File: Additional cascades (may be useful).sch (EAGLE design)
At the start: 91 parts, among them J1 S7B-PH-K

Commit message: some edits
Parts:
- removed C1, C2: 33u/50V, resistor:C-EUC0603
- removed C10, C11, C4, C6, C7, C9: 2.2u/16V, resistor:C-EUC0603
- removed C12, C14, C15, C16, C17, C18, C19, C29, C30, C44, C45: 1u/16V, resistor:C-EUC0603
- removed C13, C34, C39, C49: 2200p, resistor:C-EUC0603
- removed C20, C21, C22, C23, C24, C25: 0.1u/100V, resistor:C-EUC0603
- removed C26, C27, C31, C33, C40, C41, C43, C47, C48, C55: 0.47u/16V, resistor:C-EUC0603
- removed C28, C32, C42, C46: 0.33u/16V, resistor:C-EUC0603
- removed C3: 2.2u/10V, resistor:C-EUC0603
- removed C37, C38, C5, C8: 51p, resistor:C-EUC0603
- removed D4, D5, D6, D7, D8, D9: BAT60J, diode:BAT60J
- removed J1: S7B-PH-K, con-jst-ph:B7B-PH-K
- removed R1, R23, R24, R25, R26, R27, R28, R29: 47, resistor:R-EU_R0603
- removed R10, R11, R4, R5: 49, resistor:R-EU_R0603
- removed R17, R18, R19, R20, R21, R22: 1k, resistor:R-EU_R0603
- removed R2: 100, resistor:R-EU_R0603
- removed R3, R9: 10k, resistor:R-EU_R0603
- removed R30, R31, R32, R33, R34, R35, R36: 10, 1/4W, resistor:R-EU_R0603
- removed R6: 100k, resistor:R-EU_R0603
- removed TP1, TP2: TEST_PAD, testing:TEST_PAD
- removed U$1: BQ79606A-Q1-HTQFP(PHP)|48, texas Instrumets:BQ79606A-Q1-HTQFP(PHP)|48
- removed U$2, U$3: S4B-PH-K, con-jst-ph:S4B-PH-K
- removed U$4, U$5: PESD2CAN, stmicroelectronics:PESD2CAN
- added C35, C36: 1u/16V, resistor:C-EUC0603
- added D1: (no value), eagle-ltspice:DIODE_E-
- added Q1: BSS123, transistor-small-signal:BSS123
- added R100, R8: 100, resistor:R-EU_R0603
- added R7: 1k, resistor:R-EU_R0603
- added RB: 20, resistor:R-EU_R0603
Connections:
- removed net COMLN: C38.1, R11.1, R9.1, U$1.COMLN
- removed net COMLP: C37.2, R10.1, R9.2, U$1.COMLP
- removed net GND: C1.1, C10.2, C11.2, C12.2, C14.1, C15.1, C16.1, C17.1, C18.1, C19.1, C2.2, C3.2, C37.1, C38.2, C4.2, C40.1, C5.1, C55.1, C6.2, C7.2, C8.2, C9.2, D4.A, D5.A, D6.A, D7.A, D8.A, D9.A, J1.1, R6.1, U$1.AVSS@0, U$1.AVSS@1, U$1.CVSS, U$1.DVSS
- removed net N$1: R2.1, U$1.BAT
- removed net N$10: C22.1, C23.2, J1.4, R26.1, R33.1
- removed net N$11: C23.1, C24.2, J1.3, R27.1, R34.1
- removed net N$12: C24.1, C25.2, J1.2, R28.1, R35.1, TP1.P$1
- removed net N$13: C26.1, C27.2, C28.2, R24.2, U$1.VC5
- removed net N$14: C27.1, C28.1, C29.2, R25.2, U$1.VC4
- removed net N$15: C29.1, C30.2, R26.2, U$1.VC3
- removed net N$16: C30.1, C31.2, C32.2, R27.2, U$1.VC2
- removed net N$17: C31.1, C32.1, C33.2, R28.2, TP2.P$1, U$1.VC1
- removed net N$18: C33.1, C40.2, R29.2, U$1.VC0
- removed net N$19: C42.1, C43.1, C44.2, R32.2, U$1.CB4
- removed net N$2: R1.1, U$1.LDOIN
- removed net N$20: C44.1, C45.2, R33.2, U$1.CB3
- removed net N$21: C45.1, C46.2, C47.2, R34.2, U$1.CB2
- removed net N$22: C3.1, U$1.TSREF
- removed net N$23: C48.1, C55.2, R36.2, U$1.CB0
- removed net N$24: C41.1, C42.2, C43.2, R31.2, U$1.CB5
- removed net N$25: C25.1, R29.1, R36.1
- removed net N$26: C26.2, R23.2, U$1.VC6
- removed net N$27: C20.1, C21.2, J1.6, R24.1, R31.1
- removed net N$28: C46.1, C47.1, C48.2, R35.2, U$1.CB1
- removed net N$29: C14.2, D9.C, R17.1, U$1.GIPO1
- removed net N$3: C11.1, C7.1, C9.1, U$1.CVDD, U$1.VIO, U$1.VLDO
- removed net N$30: C19.2, D4.C, R22.1, U$1.GIPO6
- removed net N$31: C18.2, D5.C, R21.1, U$1.GIPO5
- removed net N$32: C17.2, D6.C, R20.1, U$1.GIPO4
- removed net N$33: C16.2, D7.C, R19.1, U$1.GIPO3
- removed net N$34: C15.2, D8.C, R18.1, U$1.GIPO2
- removed net N$35: C5.2, R3.2, R4.1, U$1.FAULTLP
- removed net N$36: C8.1, R3.1, R5.1, U$1.FAULTLN
- removed net N$37: C13.2, R5.2
- removed net N$38: C34.2, R4.2
- removed net N$39: C34.1, U$2.1
- removed net N$4: C6.1, U$1.AVDD
- removed net N$40: C13.1, U$2.2
- removed net N$49: C39.2, R11.2
- removed net N$5: C10.1, U$1.DVDD
- removed net N$50: C49.2, R10.2
- removed net N$51: C49.1, U$2.3
- removed net N$52: C39.1, U$2.4
- removed net N$6: C4.1, U$1.REF1
- removed net N$7: C12.1, R6.2, U$1.VPROG
- removed net N$8: C41.2, R30.2, U$1.CB6
- removed net N$9: C21.1, C22.2, J1.5, R25.1, R32.1
- removed net VCC: C1.2, C2.1, C20.2, J1.7, R1.2, R2.2, R23.1, R30.1
- new net N$41: Q1.D, RB.1
- new net N$42: R100.1, RB.2
- new net N$43: C35.2, R100.2
- new net N$44: C35.1, R7.2, R8.2
- new net N$45: C36.1, D1.C, Q1.S, R8.1
- new net N$46: C36.2, D1.A, Q1.G, R7.1
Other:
- note added: "Maximum balance current is 150mA. Connect external MOSFET to have bigger balance-current"
- note added: "external MOSFET cell balancing example"
- note removed: "Connect GIPO through 10k resistor to AVSS if unused"
- note removed: "different PCB with less than 2m wiring"
- note removed: "left COM** and FAULT** (8pins total) unconected if not used"
- note removed: "same PCB config."

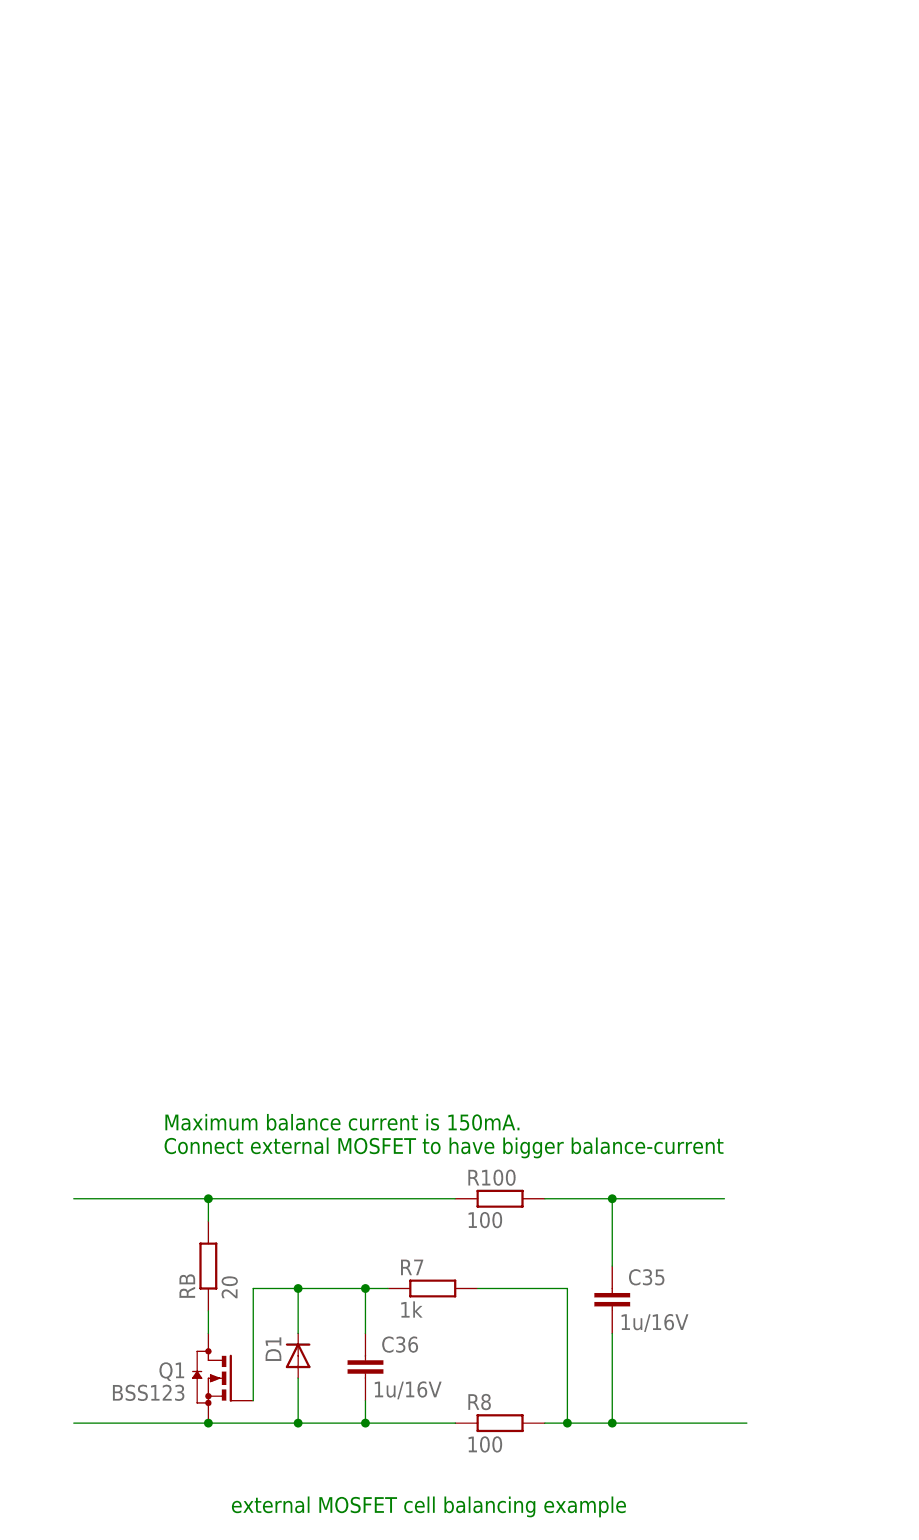
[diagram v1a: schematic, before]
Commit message: Board size to chek
The schematic file is close to release ver.
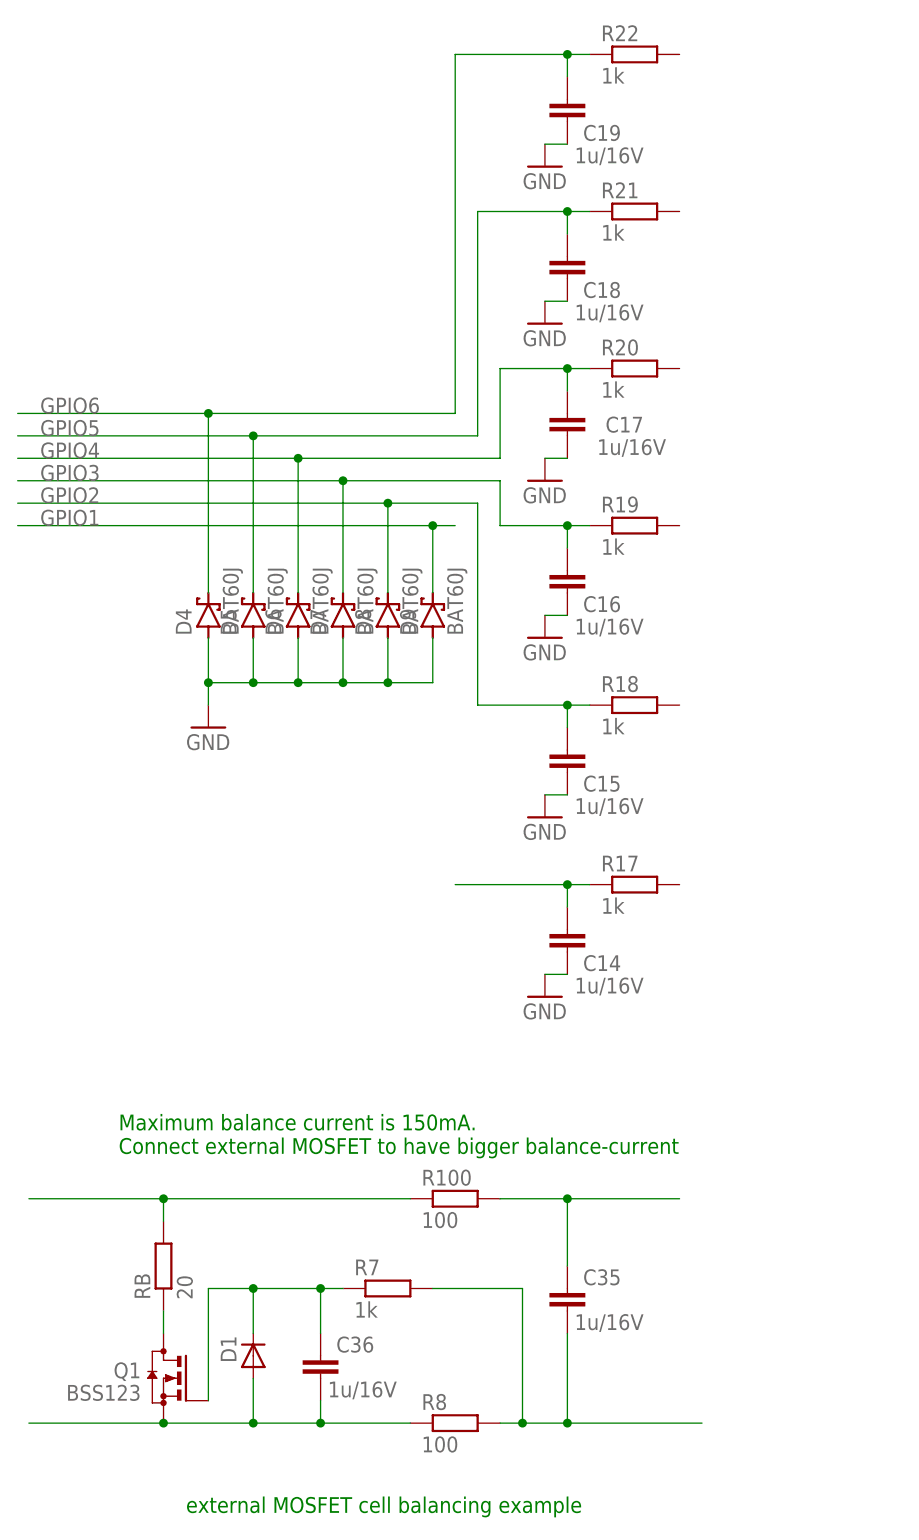
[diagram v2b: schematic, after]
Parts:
- added C14, C15, C16, C17, C18, C19: 1u/16V, resistor:C-EUC0603
- added D4, D5, D6, D7, D8, D9: BAT60J, diode:BAT60J
- added R17, R18, R19, R20, R21, R22: 1k, resistor:R-EU_R0603
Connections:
- new net GND: C14.1, C15.1, C16.1, C17.1, C18.1, C19.1, D4.A, D5.A, D6.A, D7.A, D8.A, D9.A
- new net GPIO1: C14.2, D9.C, R17.1
- new net GPIO2: C15.2, D8.C, R18.1
- new net GPIO3: C16.2, D7.C, R19.1
- new net GPIO4: C17.2, D6.C, R20.1
- new net GPIO5: C18.2, D5.C, R21.1
- new net GPIO6: C19.2, D4.C, R22.1
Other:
- moved on the sheet: C35, C36, D1, Q1, R100, R7, R8, RB

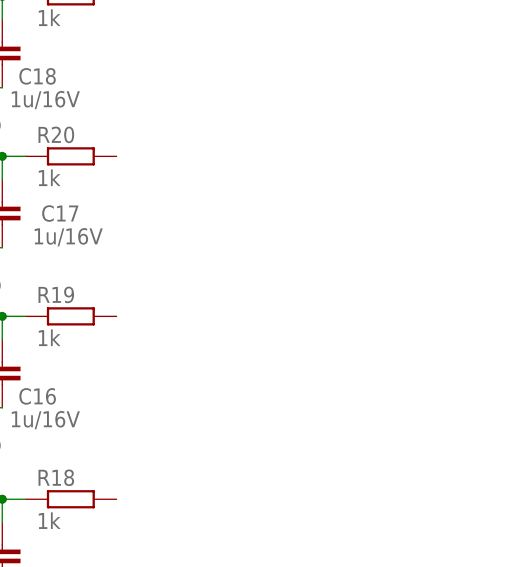
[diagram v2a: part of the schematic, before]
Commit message: Ready to generte GERBER
Silkscreen+improvements
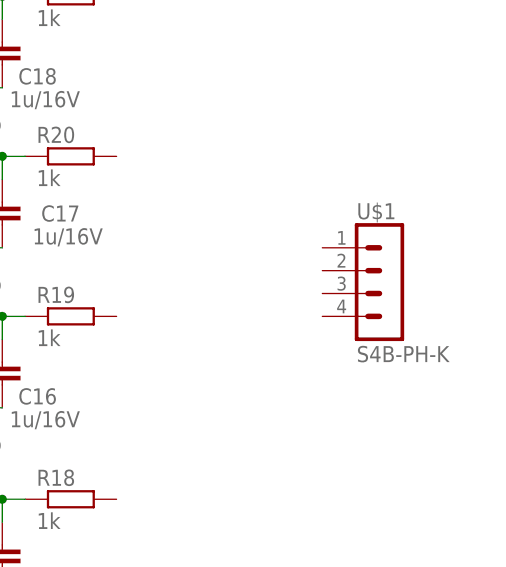
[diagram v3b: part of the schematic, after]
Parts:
- added U$1: S4B-PH-K, con-jst-ph:S4B-PH-K
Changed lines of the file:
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@@
 <?xml version="1.0" encoding="utf-8"?>
 <!DOCTYPE eagle SYSTEM "eagle.dtd">
-<eagle version="9.5.0">
+<eagle version="9.5.1">
 <drawing>
 <settings>
@@
 <part name="D9" library="diode" library_urn="urn:adsk.eagle:library:210" deviceset="BAT60J" device="" package3d_urn="urn:adsk.eagle:package:43461/1"/>
 <part name="GND22" library="supply1" library_urn="urn:adsk.eagle:library:371" deviceset="GND" device=""/>
+<part name="U$1" library="con-jst-ph" library_urn="urn:adsk.eagle:library:13143856" deviceset="S4B-PH-K" device="" package3d_urn="urn:adsk.eagle:package:13143913/2"/>
 </parts>
 <sheets>
@@
 <attribute name="VALUE" x="-60.96" y="50.8" size="1.778" layer="96"/>
 </instance>
+<instance part="U$1" gate="B" x="22.86" y="78.74" smashed="yes">
+<attribute name="NAME" x="21.59" y="86.995" size="1.778" layer="95"/>
+<attribute name="VALUE" x="21.59" y="71.12" size="1.778" layer="95"/>
+</instance>
 </instances>
